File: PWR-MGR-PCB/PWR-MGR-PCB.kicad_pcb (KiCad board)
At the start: 2 copper layers, 30 x 35 mm, 31 parts, among them J1 Conn_01x02_Pin, J2 Battery_1x2, J3 USB_C_Receptacle_USB2.0_14P, J5 Conn_01x02_Pin, U1 BQ24075, U5 USBLC6-2SC6, U6 TPS631011YBGR-Pin_Corrected

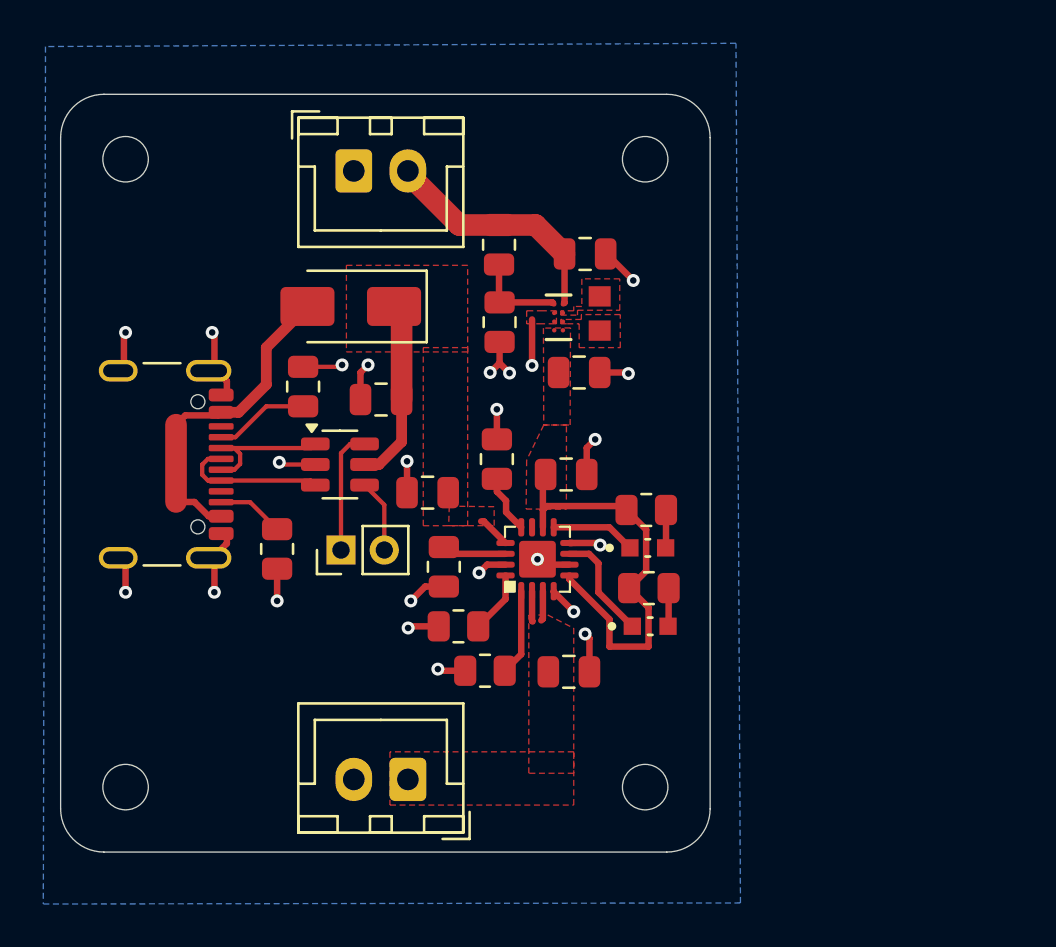
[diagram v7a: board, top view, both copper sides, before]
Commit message: Shorten traces
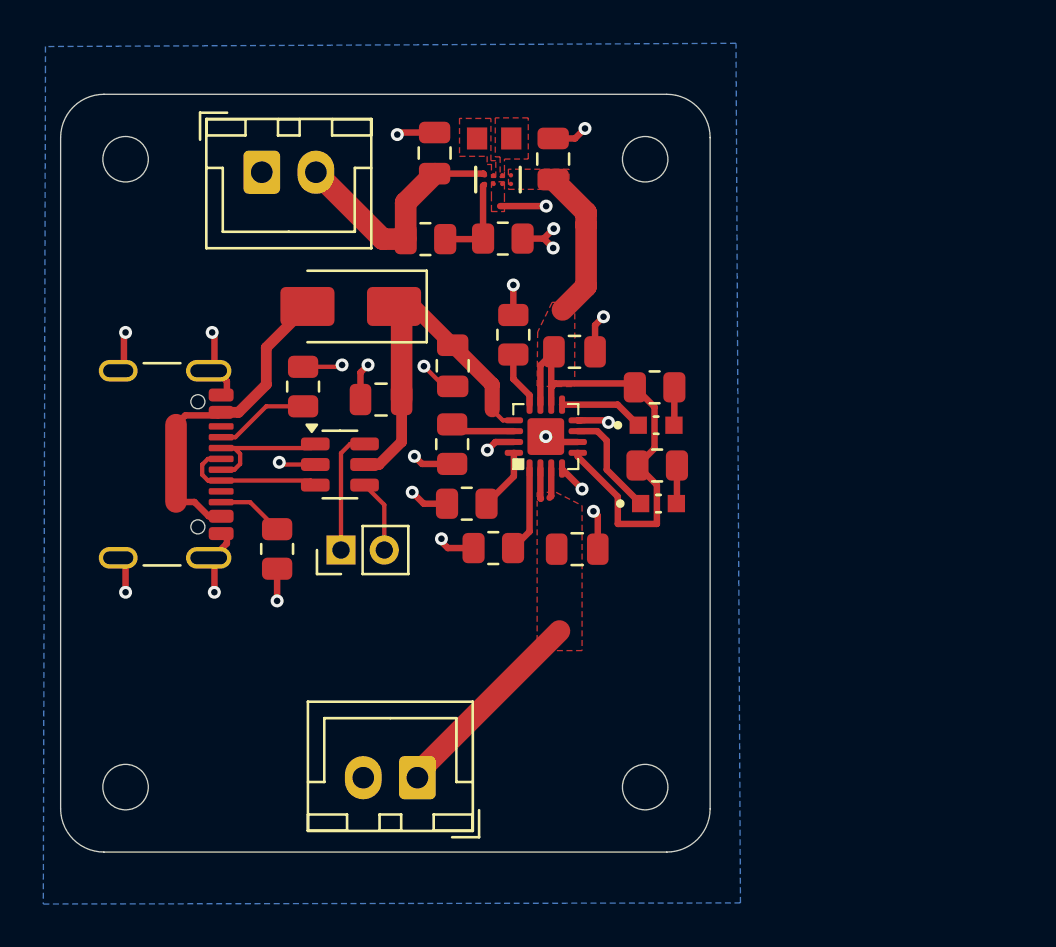
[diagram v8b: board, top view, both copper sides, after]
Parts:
- moved C9 9.93 mm to (162.8, 83.0), turned to 90 degrees
- moved L2 9.44 mm to (160.0, 82.0), turned to 0 degrees
- moved C10 8.37 mm to (157.3, 82.7), turned to 90 degrees
- moved U6 6.95 mm to (160.2, 83.9), turned to -90 degrees
- moved C5 5.97 mm to (158.1, 92.5), turned to -90 degrees
- moved R1 5.79 mm to (160.9, 91.1)
- moved C6 5.68 mm to (163.7, 91.9)
- moved R3 5.68 mm to (158.1, 96.2)
- moved R4 5.68 mm to (160.0, 101.0)
- moved R5 5.68 mm to (167.6, 97.1)
- moved D2 5.68 mm to (167.5, 95.3)
- moved R2 5.68 mm to (158.8, 98.9)
- moved R6 5.68 mm to (167.4, 93.5)
- moved C4 5.68 mm to (163.9, 101.0)
- moved D1 5.68 mm to (167.6, 98.9)
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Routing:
- net VCC_BMS: track 19.3 -> 29.1 mm
- net /PWR-MGR-01/BATT+: track 2.79 -> 12.3 mm
- net VBUS 5V: track 10.4 -> 17.3 mm
- net GND: track 41.7 -> 43.2 mm
- removed copper zone on F.Cu, net VBUS 5V
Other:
- board text added: "BATT PWR"
- board text added: "DATA"
- board text added: "PWR OUT"
